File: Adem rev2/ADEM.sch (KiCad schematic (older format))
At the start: 29 parts, among them P1 CONN_buzz, P2 CONN_01X03, P3 CONN_01X04, Q1 NPN, U3 ESP8266_THING, U4 MPU6050, U5 NVSRAM, U6 BMP180, U7 HTU21D

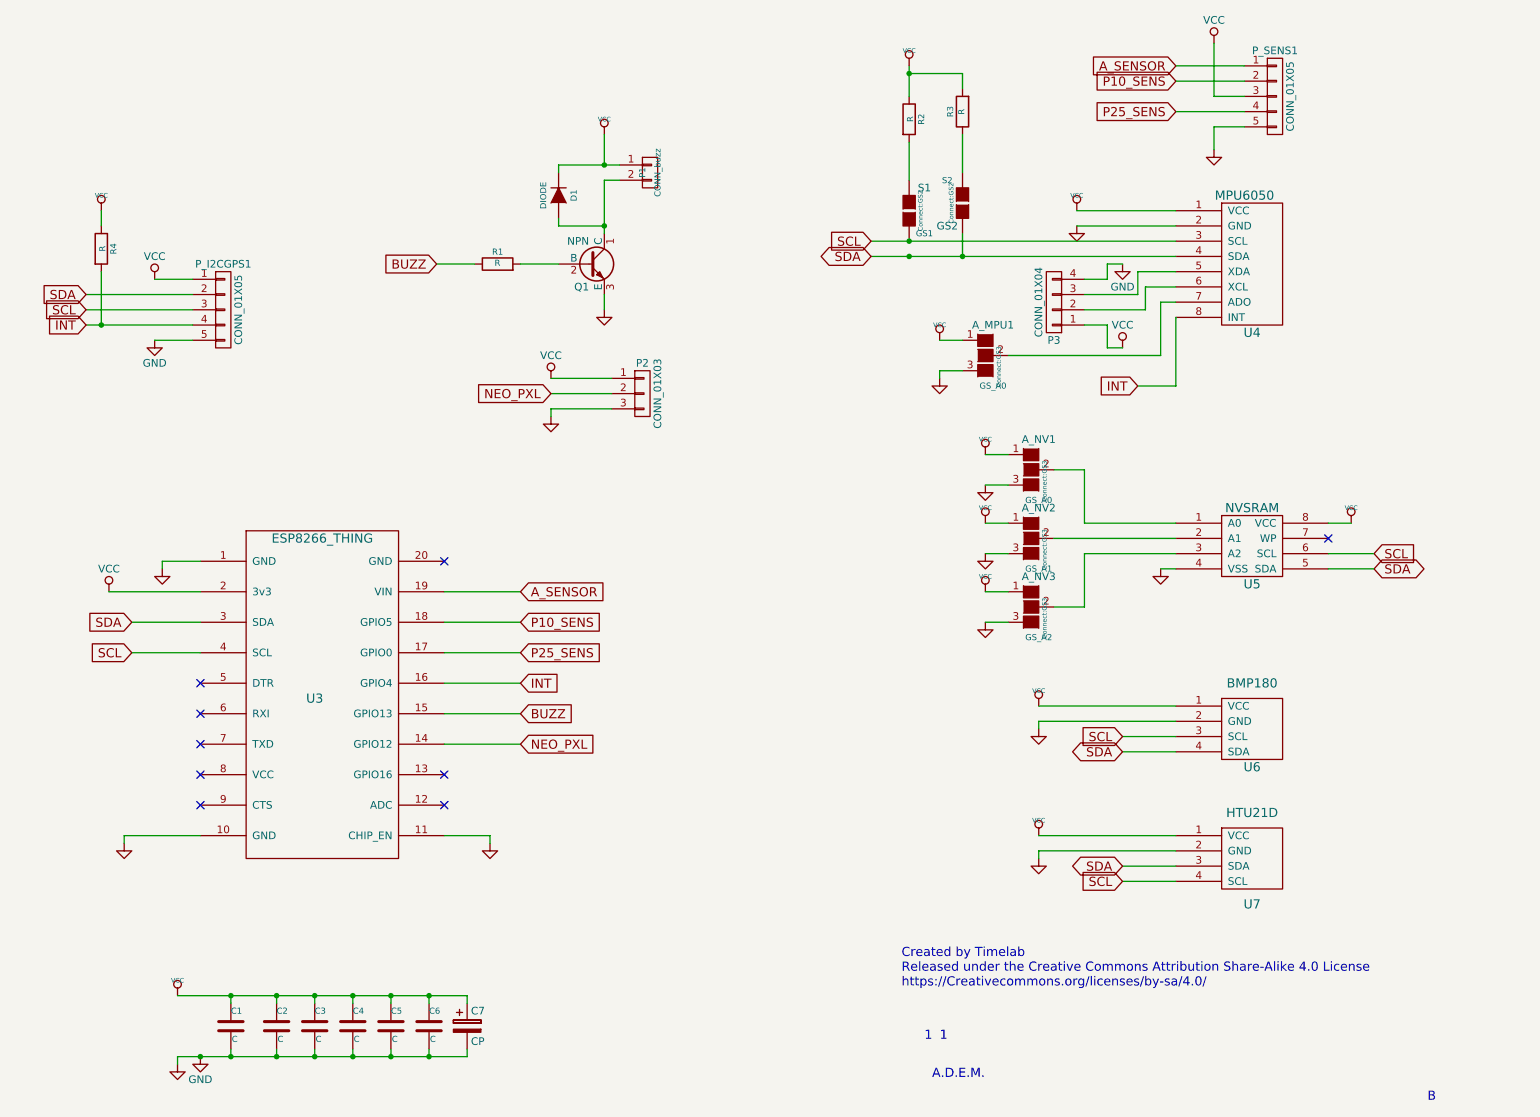
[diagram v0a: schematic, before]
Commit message: added mounting hole and fixed footprint error
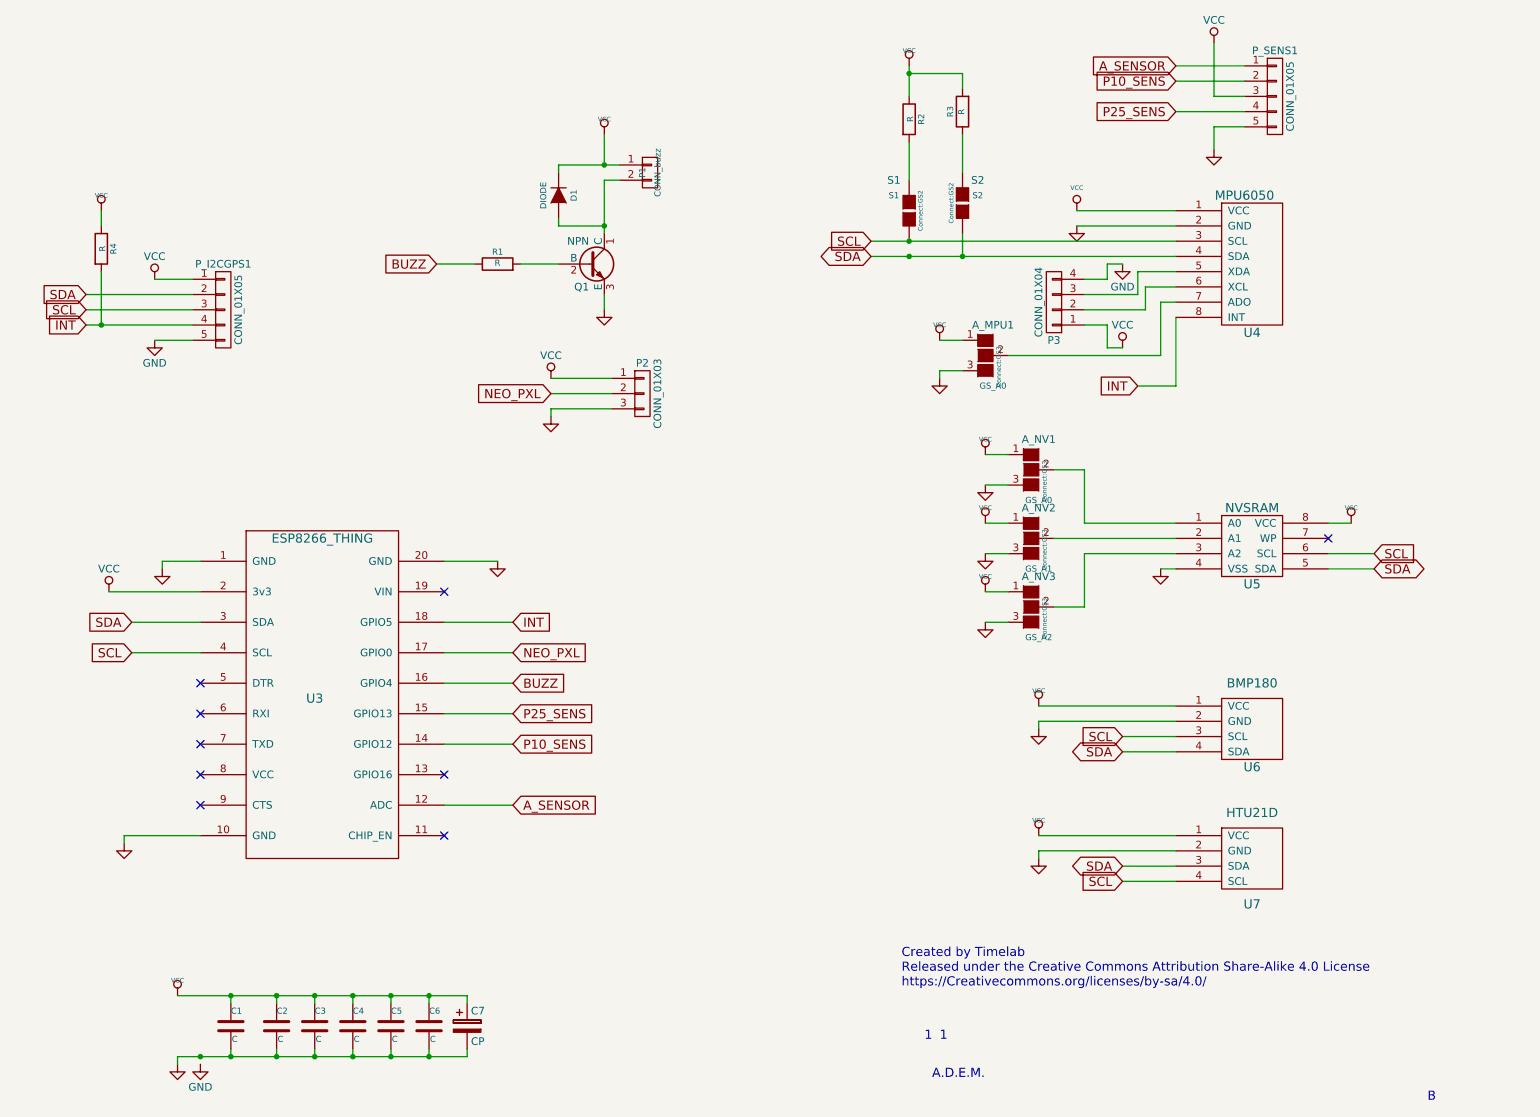
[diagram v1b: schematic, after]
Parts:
- S1: value GS1 -> S1
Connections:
- net A_SENSOR: now also U3.12 (ADC); no longer U3.19 (VIN)
- net BUZZ: now also U3.16 (GPIO4); no longer U3.15 (GPIO13)
- net GND: now also U3.20 (GND); no longer U3.11 (CHIP_EN)
- net INT: now also U3.18 (GPIO5); no longer U3.16 (GPIO4)
- net NEO_PXL: now also U3.17 (GPIO0); no longer U3.14 (GPIO12)
- net P10_SENS: now also U3.14 (GPIO12); no longer U3.18 (GPIO5)
- net P25_SENS: now also U3.15 (GPIO13); no longer U3.17 (GPIO0)

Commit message: alfa prototype
updated for first pcb prototype
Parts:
- added 5V1: 5V, Connect:PINHEAD1-2, symbol CONN_01X02
- added D2, D3: 1V8, Diodes_SMD:D_SOD-123, symbol ZENERsmall
- added R5, R6: 10K, Resistors_SMD:R_1206_HandSoldering, symbol R
- added VCC_SEL1: GS_VCC, Connect:GS3, symbol GS3
- C1, C2, C3, C4, C5, C6: value C -> 0.1µF
- C7: value CP -> 10µF
- P_SENS1: footprint Pin_Headers:Pin_Header_Angled_1x05 -> Pin_Headers:Pin_Header_Straight_1x05_Pitch2.54mm
- Q1: value NPN -> BC547
- R1, R4: value R -> 10K
- R2, R3: value R -> 2K5
- U5: value NVSRAM -> AT24C512C
- renumbered GS2 to S2
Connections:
- net GND: now also 5V1.1 (P1), R5.2, R6.2
- net P10_SENS: now also D2.1 (K); no longer U3.14 (GPIO12)
- net P25_SENS: now also D3.1 (K); no longer U3.15 (GPIO13)
- net VCC: now also VCC_SEL1.1 (G1); no longer P_SENS1.3 (P3)
- new net: P_SENS1.3 (P3), VCC_SEL1.2 (G2)
- new net: 5V1.2 (P2), VCC_SEL1.3 (G3)
- new net P10_SENS_SHFT: D2.2 (A), R5.1, U3.14 (GPIO12)
- new net P25_SENS_SHFT: D3.2 (A), R6.1, U3.15 (GPIO13)
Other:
- note added: "vcc naar stofsensor moet afgeschakeld kunnen worden. \nWe gaan SMD transistors gebruiken."
- moved on the sheet: P_I2CGPS1, P_SENS1, R4
